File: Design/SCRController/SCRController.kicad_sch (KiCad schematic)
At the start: 24 parts, among them Q1 2N2907A, Q2 2N2222A, Q3 2N2222A, Q4 2N2907A, U1 TL084, U2 TL084

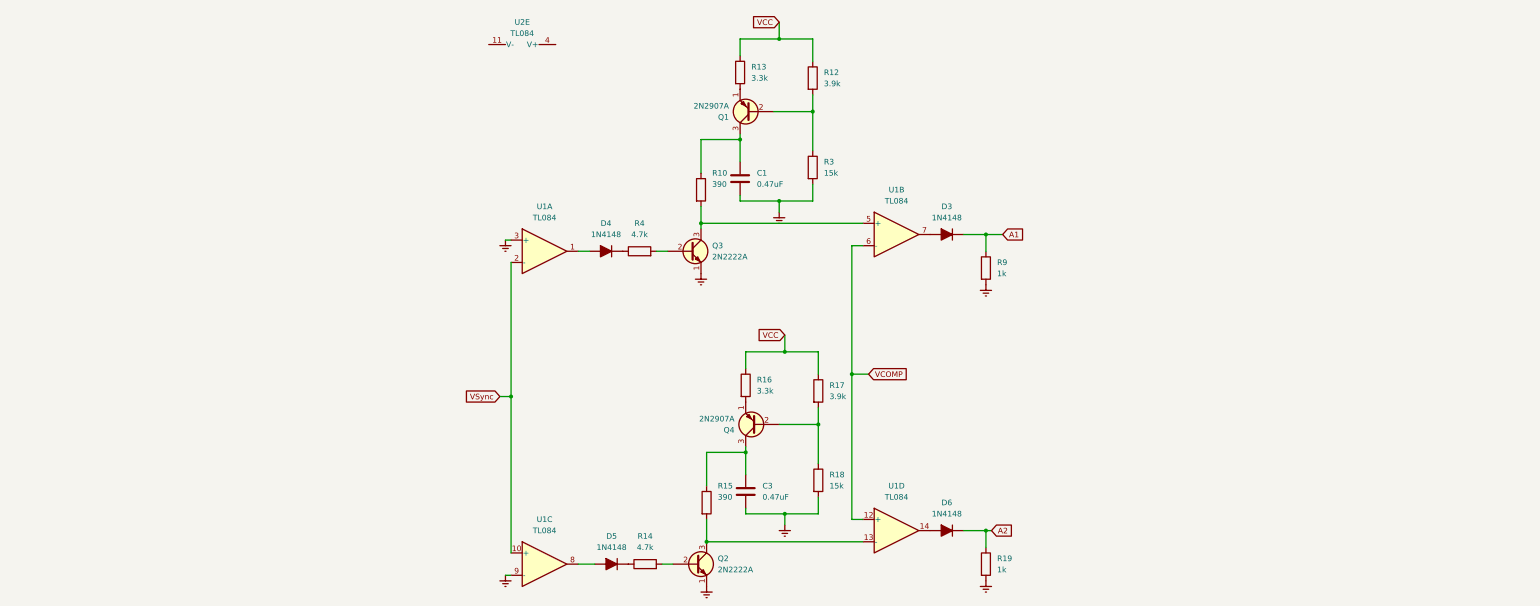
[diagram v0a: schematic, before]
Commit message: Se añadio reguladores, puente de diodos sumador y optoacoplador
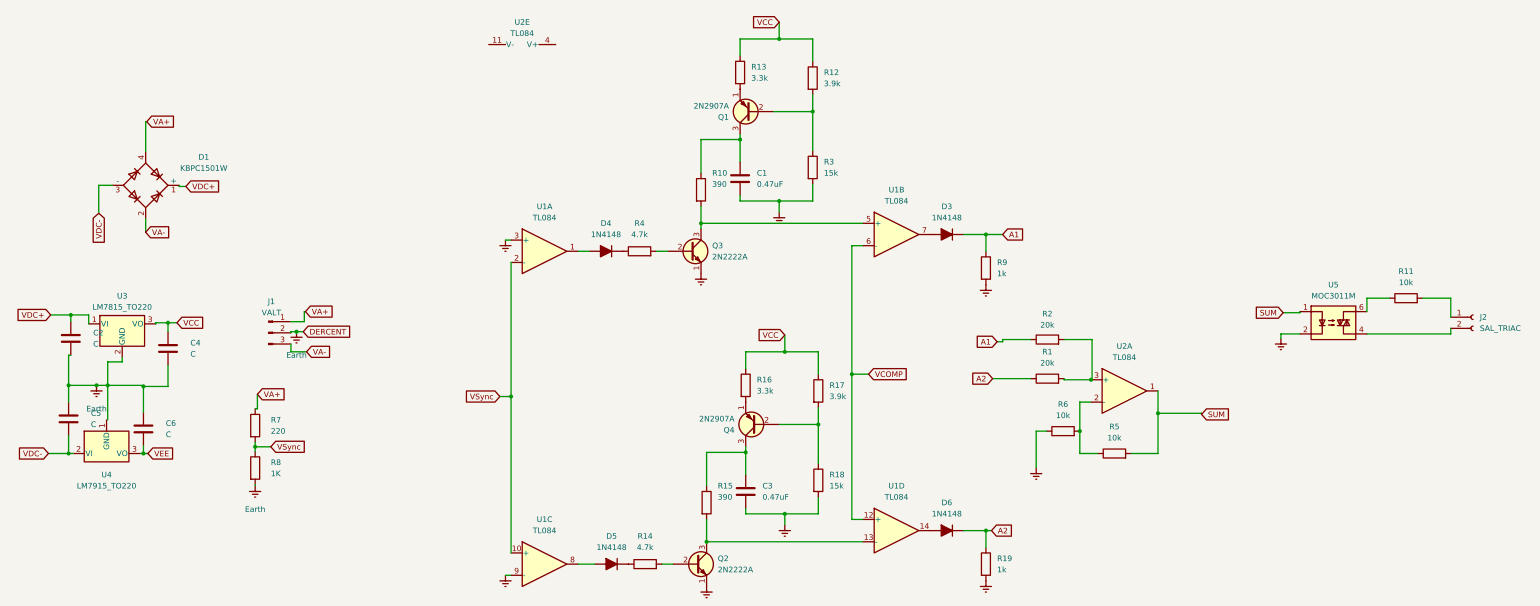
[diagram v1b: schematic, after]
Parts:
- added C2, C4, C5, C6: C, symbol Device:C
- added D1: KBPC1501W, Diode_THT:Diode_Bridge_GeneSiC_KBPC_W, symbol Diode_Bridge:KBPC1501W
- added J1: VALT, symbol Connector:Conn_01x03_Pin
- added J2: SAL_TRIAC, symbol Connector:Conn_01x02_Socket
- added R1, R2: 20k, symbol Device:R
- added R11, R5, R6: 10k, symbol Device:R
- added R7: 220, symbol Device:R
- added R8: 1K, symbol Device:R
- added unit 1 of U2
- added U3: LM7815_TO220, Package_TO_SOT_THT:TO-220-3_Vertical, symbol Regulator_Linear:LM7815_TO220
- added U4: LM7915_TO220, Package_TO_SOT_THT:TO-220-3_Vertical, symbol Regulator_Linear:LM7915_TO220
- added U5: MOC3011M, symbol Relay_SolidState:MOC3011M
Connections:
- net A1: now also R2.1
- net A2: now also R1.1
- net Earth: now also C2.2, C4.2, C5.1, C6.1, J1.2 (Pin_2), R6.1, R8.2, U3.2 (GND), U5.2
- net VCC: now also C4.1, U3.3 (VO)
- net VSync: now also R7.2, R8.1
- new net: R5.1, R6.2, U2.2 (-)
- new net: R1.2, R2.2, U2.3 (+)
- new net: R11.1, U5.6
- new net: J2.1 (Pin_1), R11.2
- new net: J2.2 (Pin_2), U5.4
- new net SUM: R5.2, U2.1, U5.1
- new net VA+: D1.4, J1.1 (Pin_1), R7.1
- new net VA-: D1.2, J1.3 (Pin_3)
- new net VDC+: C2.1, D1.1 (+), U3.1 (VI)
- new net VDC-: C5.2, D1.3 (-), U4.2 (VI)
- new net VEE: C6.2, U4.3 (VO)

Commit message: Añadio alimentacion opamps
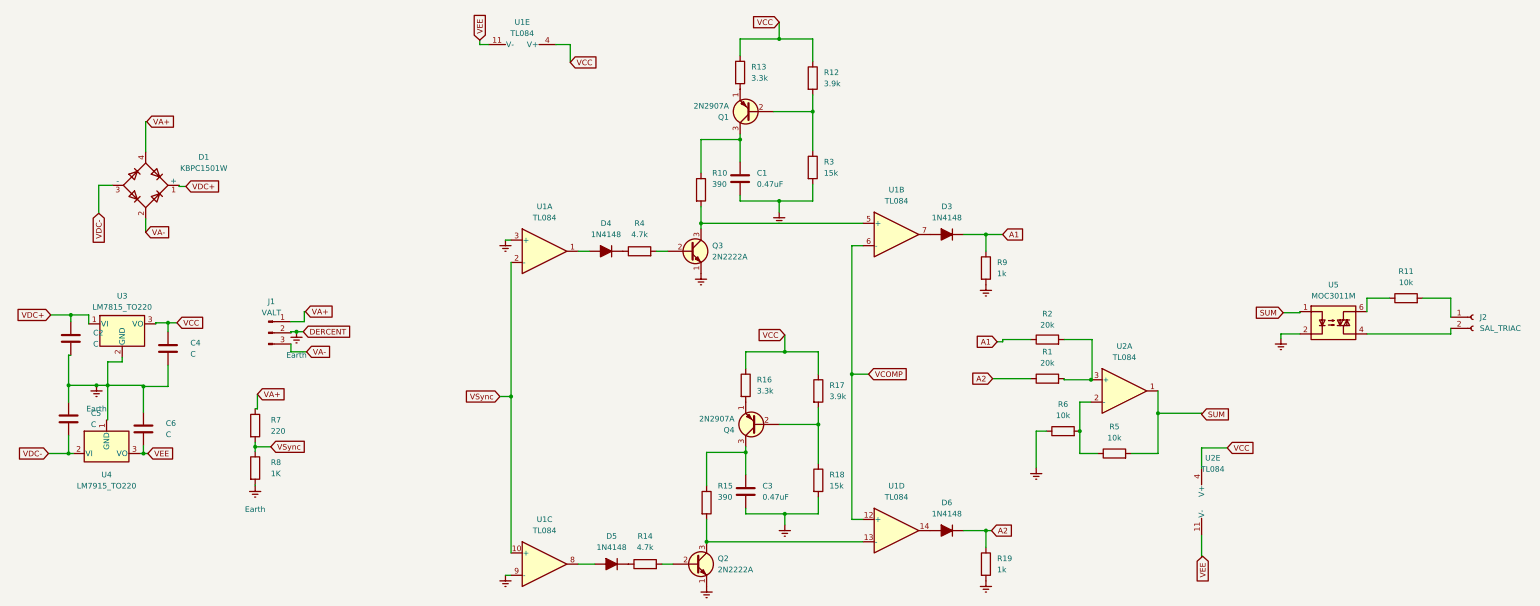
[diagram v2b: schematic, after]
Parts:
- added unit 5 of U2
- renumbered U2 to U1
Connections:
- net VCC: now also U1.4 (V+), U2.4 (V+)
- net VEE: now also U1.11 (V-), U2.11 (V-)
